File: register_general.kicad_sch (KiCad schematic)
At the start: 29 parts, among them J1 Conn_01x16_Pin, J2 Conn_01x16_Pin, J3 load select, J4 output select, U1 74HC245, U2 74HC377

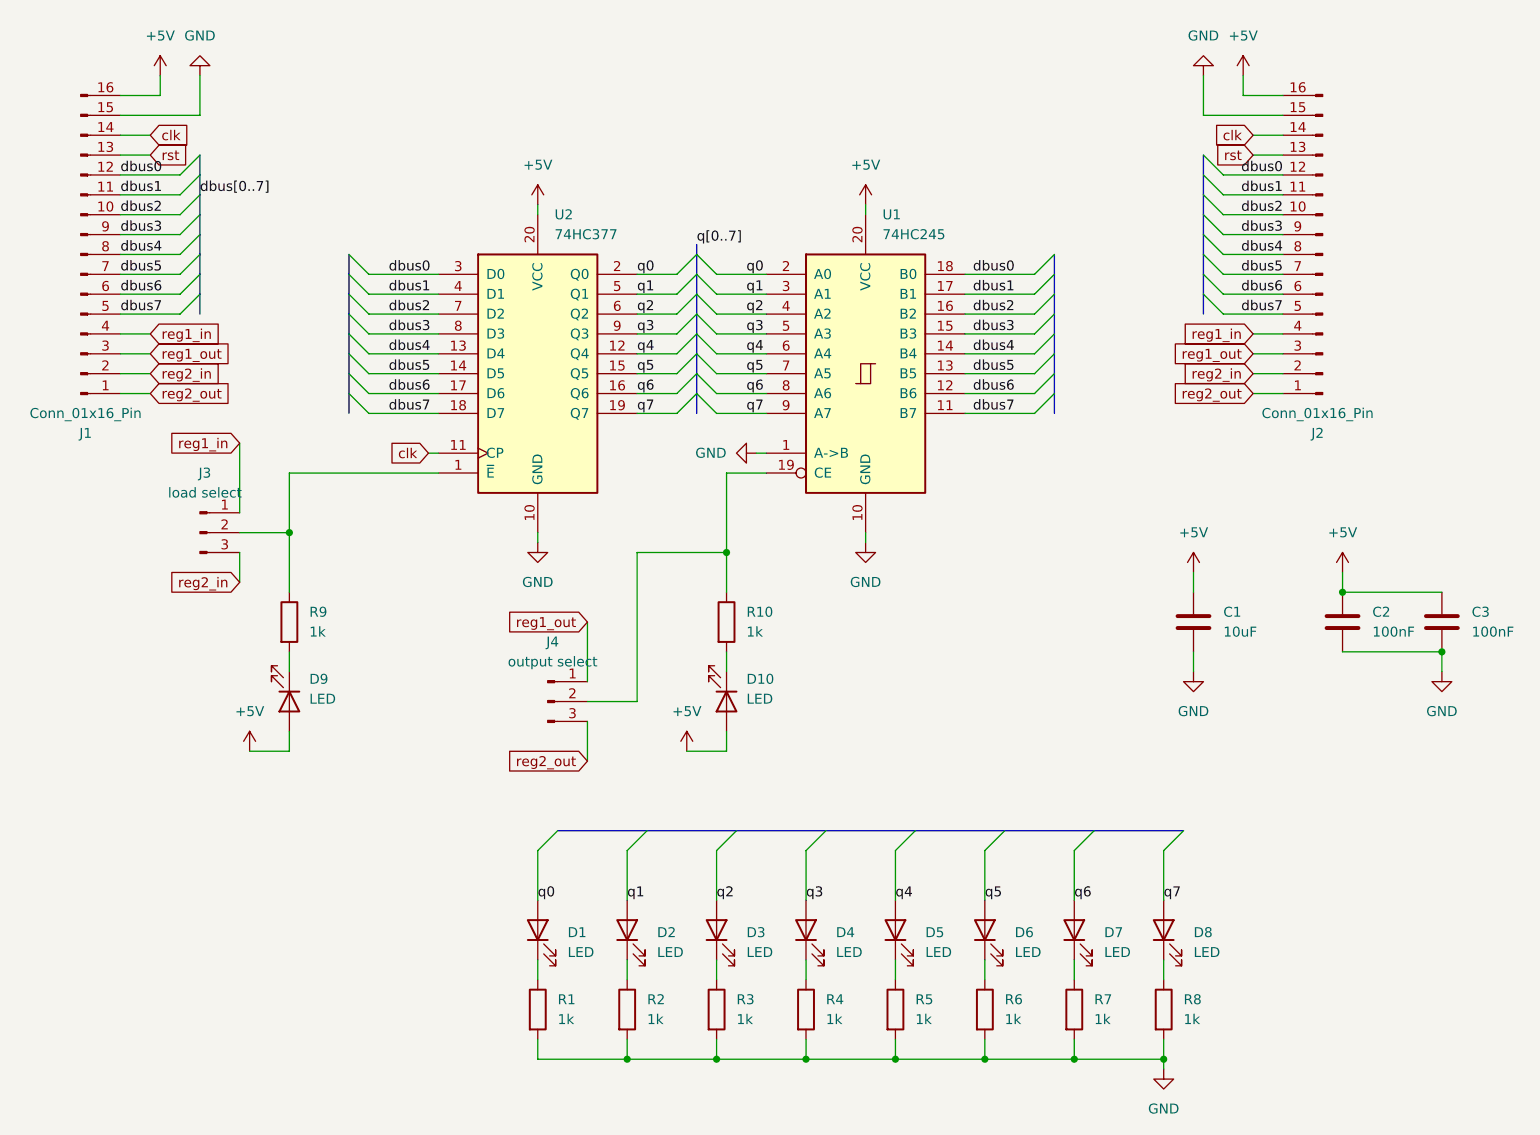
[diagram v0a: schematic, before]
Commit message: Add vias, GND planes, QR code, version and other details
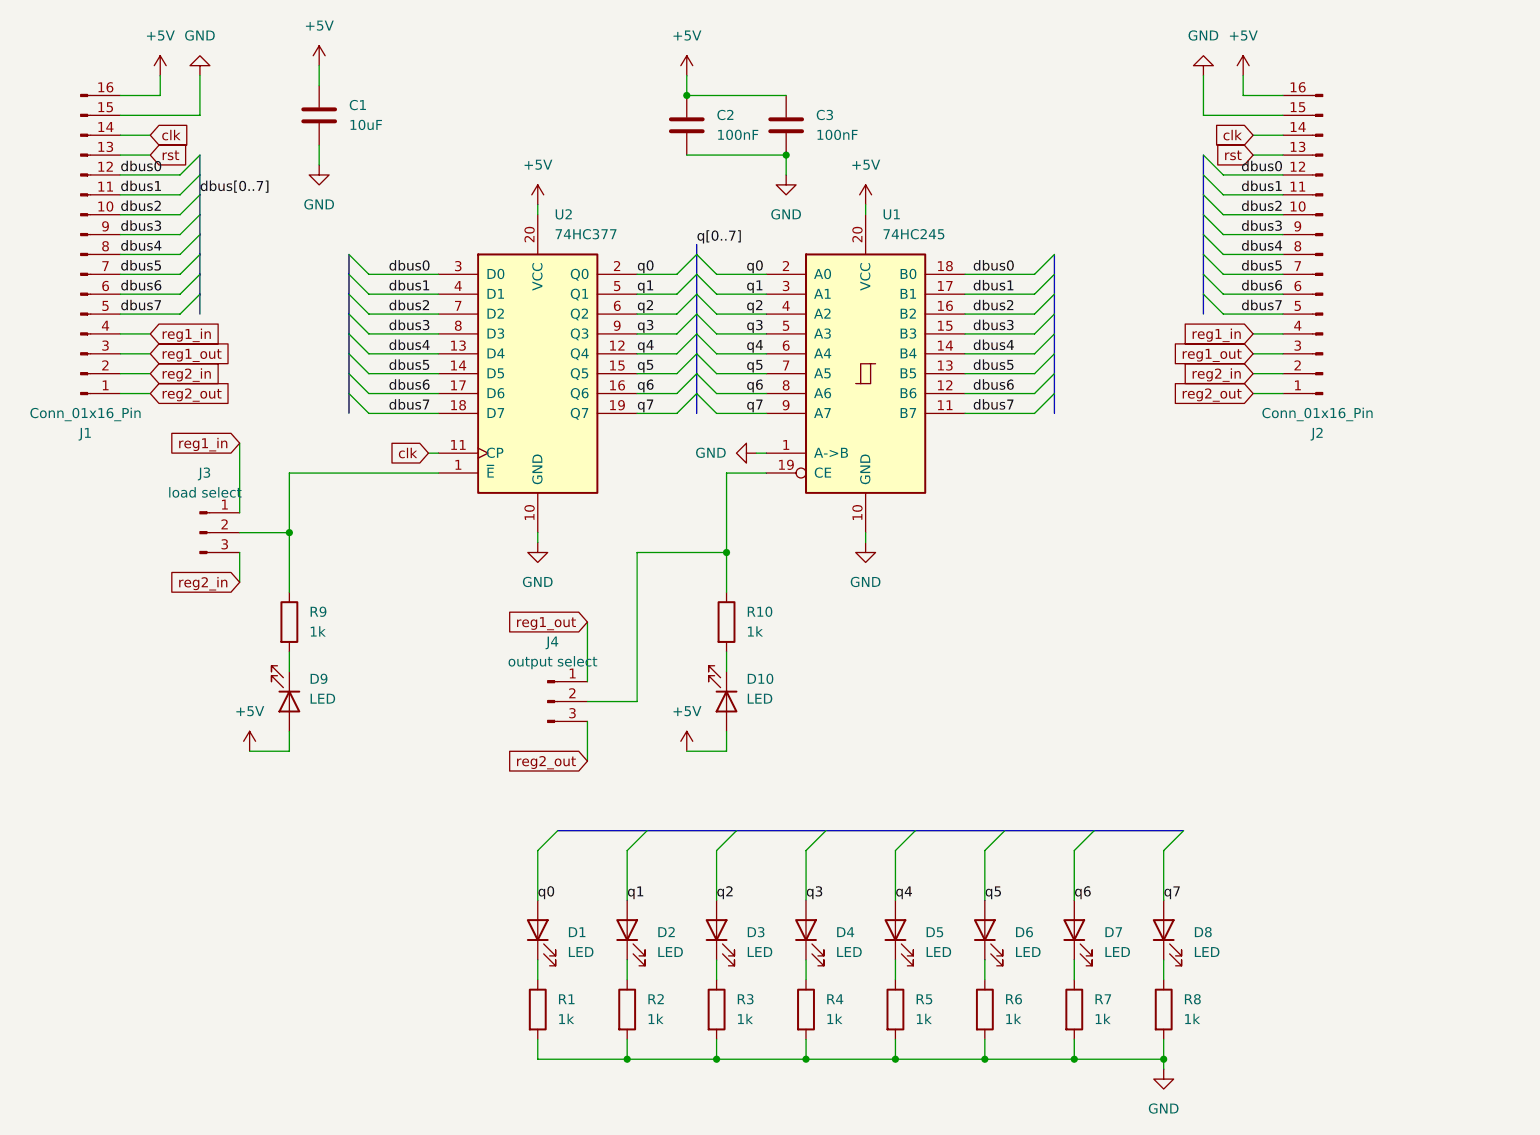
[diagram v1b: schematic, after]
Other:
- moved on the sheet: C1, C2, C3
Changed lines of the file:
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@@
 	(paper "A4")
 	(junction
-		(at 191.77 97.79)
+		(at 107.95 34.29)
 		(diameter 0)
 		(color 0 0 0 0)
@@
 	)
 	(junction
-		(at 204.47 105.41)
+		(at 120.65 41.91)
 		(diameter 0)
 		(color 0 0 0 0)
@@
 	(wire
 		(pts
-			(xy 204.47 105.41) (xy 204.47 107.95)
+			(xy 120.65 41.91) (xy 120.65 44.45)
 		)
 		(stroke
@@
 	(wire
 		(pts
-			(xy 191.77 95.25) (xy 191.77 97.79)
+			(xy 107.95 31.75) (xy 107.95 34.29)
 		)
 		(stroke
@@
 	(wire
 		(pts
-			(xy 191.77 105.41) (xy 204.47 105.41)
+			(xy 107.95 41.91) (xy 120.65 41.91)
 		)
 		(stroke
@@
 	(wire
 		(pts
-			(xy 172.72 95.25) (xy 172.72 97.79)
+			(xy 60.96 30.48) (xy 60.96 33.02)
 		)
 		(stroke
@@
 	(wire
 		(pts
-			(xy 172.72 105.41) (xy 172.72 107.95)
+			(xy 60.96 40.64) (xy 60.96 43.18)
 		)
 		(stroke
@@
 	(wire
 		(pts
-			(xy 191.77 97.79) (xy 204.47 97.79)
+			(xy 107.95 34.29) (xy 120.65 34.29)
 		)
 		(stroke
@@
 	(symbol
 		(lib_id "power:+5V")
-		(at 172.72 95.25 0)
+		(at 60.96 30.48 0)
 		(unit 1)
 		(exclude_from_sim no)
@@
 		(fields_autoplaced yes)
 		(property "Reference" "#PWR020"
-			(at 172.72 99.06 0)
+			(at 60.96 34.29 0)
 			(effects
 				(font
@@
 		)
 		(property "Value" "+5V"
-			(at 172.72 90.17 0)
+			(at 60.96 25.4 0)
 			(effects
 				(font
@@
 		)
 		(property "Footprint" ""
-			(at 172.72 95.25 0)
+			(at 60.96 30.48 0)
 			(effects
 				(font
@@
 		)
 		(property "Datasheet" ""
-			(at 172.72 95.25 0)
+			(at 60.96 30.48 0)
 			(effects
 				(font
@@
 		)
 		(property "Description" "Power symbol creates a global label with name \"+5V\""
-			(at 172.72 95.25 0)
+			(at 60.96 30.48 0)
 			(effects
 				(font
@@
 	(symbol
 		(lib_id "power:GND")
-		(at 204.47 107.95 0)
+		(at 120.65 44.45 0)
 		(unit 1)
 		(exclude_from_sim no)
@@
 		(fields_autoplaced yes)
 		(property "Reference" "#PWR023"
-			(at 204.47 114.3 0)
+			(at 120.65 50.8 0)
 			(effects
 				(font
@@
 		)
 		(property "Value" "GND"
-			(at 204.47 113.03 0)
+			(at 120.65 49.53 0)
 			(effects
 				(font
@@
 		)
 		(property "Footprint" ""
-			(at 204.47 107.95 0)
+			(at 120.65 44.45 0)
 			(effects
 				(font
@@
 		)
 		(property "Datasheet" ""
-			(at 204.47 107.95 0)
+			(at 120.65 44.45 0)
 			(effects
 				(font
@@
 		)
 		(property "Description" "Power symbol creates a global label with name \"GND\" , ground"
-			(at 204.47 107.95 0)
+			(at 120.65 44.45 0)
 			(effects
 				(font
@@
 	(symbol
 		(lib_id "Device:C")
-		(at 204.47 101.6 0)
+		(at 120.65 38.1 0)
 		(unit 1)
 		(exclude_from_sim no)
@@
 		(fields_autoplaced yes)
 		(property "Reference" "C3"
-			(at 208.28 100.3299 0)
+			(at 124.46 36.8299 0)
 			(effects
 				(font
@@
 		)
 		(property "Value" "100nF"
-			(at 208.28 102.8699 0)
+			(at 124.46 39.3699 0)
 			(effects
 				(font
@@
 		)
 		(property "Footprint" "Capacitor_SMD:C_0805_2012Metric"
-			(at 205.4352 105.41 0)
+			(at 121.6152 41.91 0)
 			(effects
 				(font
@@
 		)
 		(property "Datasheet" "~"
-			(at 204.47 101.6 0)
+			(at 120.65 38.1 0)
 			(effects
 				(font
@@
 		)
 		(property "Description" "Unpolarized capacitor"
-			(at 204.47 101.6 0)
+			(at 120.65 38.1 0)
 			(effects
 				(font
@@
 	(symbol
 		(lib_id "power:GND")
-		(at 172.72 107.95 0)
+		(at 60.96 43.18 0)
 		(unit 1)
 		(exclude_from_sim no)
@@
 		(fields_autoplaced yes)
 		(property "Reference" "#PWR022"
-			(at 172.72 114.3 0)
+			(at 60.96 49.53 0)
 			(effects
 				(font
@@
 		)
 		(property "Value" "GND"
-			(at 172.72 113.03 0)
+			(at 60.96 48.26 0)
 			(effects
 				(font
@@
 		)
 		(property "Footprint" ""
-			(at 172.72 107.95 0)
+			(at 60.96 43.18 0)
 			(effects
 				(font
@@
 		)
 		(property "Datasheet" ""
-			(at 172.72 107.95 0)
+			(at 60.96 43.18 0)
 			(effects
 				(font
@@
 		)
 		(property "Description" "Power symbol creates a global label with name \"GND\" , ground"
-			(at 172.72 107.95 0)
+			(at 60.96 43.18 0)
 			(effects
 				(font
@@
 	(symbol
 		(lib_id "Device:C")
-		(at 172.72 101.6 0)
+		(at 60.96 36.83 0)
 		(unit 1)
 		(exclude_from_sim no)
@@
 		(fields_autoplaced yes)
 		(property "Reference" "C1"
-			(at 176.53 100.3299 0)
+			(at 64.77 35.5599 0)
 			(effects
 				(font
@@
 		)
 		(property "Value" "10uF"
-			(at 176.53 102.8699 0)
+			(at 64.77 38.0999 0)
 			(effects
 				(font
@@
 		)
 		(property "Footprint" "Capacitor_SMD:C_0805_2012Metric"
-			(at 173.6852 105.41 0)
+			(at 61.9252 40.64 0)
 			(effects
 				(font
@@
 		)
 		(property "Datasheet" "~"
-			(at 172.72 101.6 0)
+			(at 60.96 36.83 0)
 			(effects
 				(font
@@
 		)
 		(property "Description" "Unpolarized capacitor"
-			(at 172.72 101.6 0)
+			(at 60.96 36.83 0)
 			(effects
 				(font
@@
 	(symbol
 		(lib_id "power:+5V")
-		(at 191.77 95.25 0)
+		(at 107.95 31.75 0)
 		(unit 1)
 		(exclude_from_sim no)
@@
 		(fields_autoplaced yes)
 		(property "Reference" "#PWR021"
-			(at 191.77 99.06 0)
+			(at 107.95 35.56 0)
 			(effects
 				(font
@@
 		)
 		(property "Value" "+5V"
-			(at 191.77 90.17 0)
+			(at 107.95 26.67 0)
 			(effects
 				(font
@@
 		)
 		(property "Footprint" ""
-			(at 191.77 95.25 0)
+			(at 107.95 31.75 0)
 			(effects
 				(font
@@
 		)
 		(property "Datasheet" ""
-			(at 191.77 95.25 0)
+			(at 107.95 31.75 0)
 			(effects
 				(font
@@
 		)
 		(property "Description" "Power symbol creates a global label with name \"+5V\""
-			(at 191.77 95.25 0)
+			(at 107.95 31.75 0)
 			(effects
 				(font
@@
 	(symbol
 		(lib_id "Device:C")
-		(at 191.77 101.6 0)
+		(at 107.95 38.1 0)
 		(unit 1)
 		(exclude_from_sim no)
@@
 		(fields_autoplaced yes)
 		(property "Reference" "C2"
-			(at 195.58 100.3299 0)
+			(at 111.76 36.8299 0)
 			(effects
 				(font
@@
 		)
 		(property "Value" "100nF"
-			(at 195.58 102.8699 0)
+			(at 111.76 39.3699 0)
 			(effects
 				(font
@@
 		)
 		(property "Footprint" "Capacitor_SMD:C_0805_2012Metric"
-			(at 192.7352 105.41 0)
+			(at 108.9152 41.91 0)
 			(effects
 				(font
@@
 		)
 		(property "Datasheet" "~"
-			(at 191.77 101.6 0)
+			(at 107.95 38.1 0)
 			(effects
 				(font
@@
 		)
 		(property "Description" "Unpolarized capacitor"
-			(at 191.77 101.6 0)
+			(at 107.95 38.1 0)
 			(effects
 				(font
